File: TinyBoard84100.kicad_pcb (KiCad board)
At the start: 2 copper layers, 14 parts, among them P1 CONN_01X02, P2 CONN_01X07, P3 CONN_01X07, P4 CONN_02X03, SW1 SW_PUSH, U1 78L05, U2 ATTINY841

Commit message: First layout
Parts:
- C1, R1, R2, R3, U1: moved to B.Cu
- moved SW1 37.6 mm to (172.7, 80.0), turned to 270 degrees
- moved C2 35.2 mm to (158.8, 80.0), turned to 90 degrees
- moved R1 33.5 mm to (171.4, 80.0)
- moved C1 33.2 mm to (158.8, 80.0), turned to 90 degrees
- moved U1 29.6 mm to (165.1, 80.0), turned to 180 degrees
- moved U2 29.0 mm to (165.1, 80.0), turned to 90 degrees
- moved D1 28.1 mm to (179.1, 73.7), turned to 180 degrees
- moved P4 25.6 mm to (177.8, 77.5)
- moved R2 24.2 mm to (178.8, 74.4), turned to 180 degrees
- moved P1 24.1 mm to (154.9, 81.3), turned to 180 degrees
- moved R3 24.0 mm to (176.8, 86.4)
- moved P3 20.7 mm to (157.5, 73.7), turned to 90 degrees
- moved D2 18.6 mm to (179.1, 86.4)
- moved P2 6.22 mm to (157.5, 86.4), turned to 90 degrees
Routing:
- net /PA4: track 0.00 -> 22.6 mm, vias 0 -> 1
- net /PB3: track 0.00 -> 22.5 mm, vias 0 -> 2
- net /PA6: track 0.00 -> 16.9 mm, vias 0 -> 1
- net GND: track 0.00 -> 13.4 mm, vias 0 -> 4
- net /PA5: track 0.00 -> 12.0 mm
- net Net-(C1-Pad1): track 0.00 -> 9.79 mm, vias 0 -> 1
- net +5V: track 0.00 -> 8.70 mm, vias 0 -> 1
- net /PA7: track 0.00 -> 4.70 mm
- net /PB0: track 0.00 -> 4.70 mm
- net /PA0: track 0.00 -> 4.70 mm
- net Net-(D1-Pad1): track 0.00 -> 4.64 mm, vias 0 -> 1
- net /PA1: track 0.00 -> 4.18 mm
- net /PB1: track 0.00 -> 4.18 mm
- net /PA3: track 0.00 -> 4.18 mm
- net /PB2: track 0.00 -> 4.18 mm
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- added copper zone on F.Cu, net +5V
- added copper zone on B.Cu, net GND
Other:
- board outline added: 27.9 x 15.2 mm

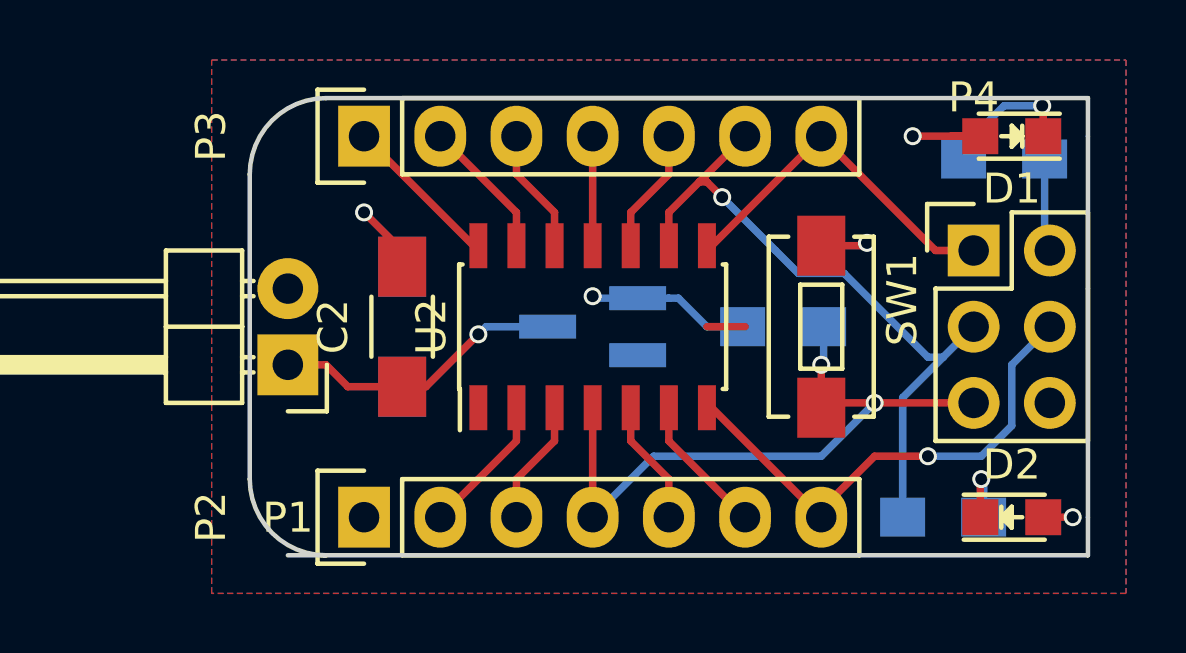
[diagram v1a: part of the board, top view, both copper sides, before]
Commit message: fixed zone connections
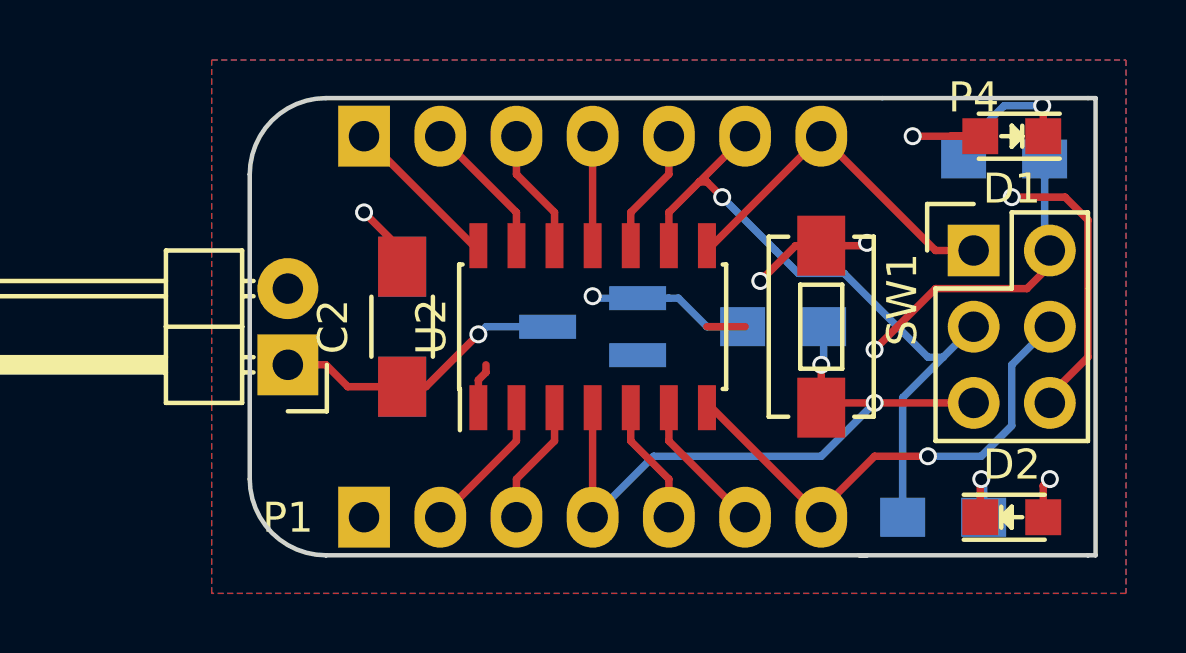
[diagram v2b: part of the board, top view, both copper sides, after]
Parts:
- P2, P3: moved to B.Cu
- turned P2 to 270 degrees
- turned P3 to 270 degrees
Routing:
- net GND: track 13.4 -> 25.8 mm, vias 4 -> 6
- net +5V: track 8.70 -> 17.7 mm, vias 1 -> 2
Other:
- board size 27.9 x 15.2 mm -> 28.2 x 15.2 mm

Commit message: gerbers
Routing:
- net (no net): track 1.27 -> 0.00 mm
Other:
- board text added: "+ -"
- board text added: "5V"
- board text added: "GND"
- board text added: "PA0"
- board text added: "PA1"
- board text added: "PA2"
- board text added: "PA3"
- board text added: "PA4"
- board text added: "PA5"
- board text added: "PA6"
- board text added: "PA7"
- board text added: "PB0"
- board text added: "PB1"
- board text added: "PB2"
- board text added: "PB3"
- board text added: "TinyBoard84100"

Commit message: silkscreen edits
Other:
- board text added: "+"
- board text added: "-"
- board text added: "TinyBoard84100 Unregulated Powersupply Rev2"
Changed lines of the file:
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@@
     (links 38)
     (no_connects 1)
-    (area 143.810667 68.875 185.453143 91.393333)
+    (area 153.594999 72.314999 181.939001 87.705001)
     (thickness 1.6)
-    (drawings 26)
+    (drawings 29)
     (tracks 119)
     (zones 0)
@@
   (page A4)
   (layers
-    (0 F.Cu signal hide)
-    (31 B.Cu signal hide)
+    (0 F.Cu signal)
+    (31 B.Cu signal)
     (32 B.Adhes user hide)
     (33 F.Adhes user hide)
@@
     (tags "LED 0805 SMD")
     (attr smd)
-    (fp_text reference D1 (at 2.54 0.254 180) (layer F.SilkS)
+    (fp_text reference D1 (at 0 2.032 180) (layer F.SilkS)
       (effects (font (size 1 1) (thickness 0.15)))
     )
@@
     (tags "LED 0805 SMD")
     (attr smd)
-    (fp_text reference D2 (at 0 -1.524) (layer F.SilkS)
+    (fp_text reference D2 (at -2.54 2.54) (layer F.SilkS)
       (effects (font (size 1 1) (thickness 0.15)))
     )
@@
     )
   )
+  (gr_text - (at 180.594 84.328) (layer F.SilkS)
+    (effects (font (size 0.762 0.762) (thickness 0.1905)))
+  )
+  (gr_text + (at 180.34 75.692) (layer F.SilkS)
+    (effects (font (size 0.762 0.762) (thickness 0.1905)))
+  )
+  (gr_text "TinyBoard84100\nUnregulated\nPowersupply\nRev2" (at 167.894 80.264) (layer B.SilkS)
+    (effects (font (thickness 0.3048)) (justify mirror))
+  )
   (gr_text "+  -" (at 156.972 80.01 90) (layer F.SilkS)

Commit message: minimizing
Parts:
- removed P1: CONN_01X02, Pin_Headers:Pin_Header_Angled_1x02
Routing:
- net Net-(C1-Pad1): track 9.79 -> 5.68 mm
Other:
- board size 28.2 x 15.2 mm -> 25.7 x 15.2 mm
- board text removed: "+ -"
- board text removed: "TinyBoard84100 Unregulated Powersupply Rev2"
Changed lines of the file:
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@@
 (kicad_pcb (version 4) (host pcbnew 4.0.5+dfsg1-4)
   (general
-    (links 38)
+    (links 36)
     (no_connects 1)
-    (area 153.594999 72.314999 181.939001 87.705001)
+    (area 156.134999 72.314999 181.939001 87.705001)
     (thickness 1.6)
-    (drawings 29)
-    (tracks 119)
+    (drawings 26)
+    (tracks 116)
     (zones 0)
-    (modules 14)
+    (modules 13)
     (nets 18)
   )
   (page A4)
   (layers
-    (0 F.Cu signal)
-    (31 B.Cu signal)
+    (0 F.Cu signal hide)
+    (31 B.Cu signal hide)
     (32 B.Adhes user hide)
     (33 F.Adhes user hide)
@@
     (35 F.Paste user hide)
     (36 B.SilkS user)
-    (37 F.SilkS user)
+    (37 F.SilkS user hide)
     (38 B.Mask user hide)
     (39 F.Mask user hide)
@@
     (pad_to_mask_clearance 0.2)
     (aux_axis_origin 0 0)
-    (grid_origin 153.924 72.644)
+    (grid_origin 156.21 72.39)
     (visible_elements FFFFFF7F)
     (pcbplotparams
@@
       (scale (xyz 1 1 1))
       (rotate (xyz 0 0 0))
-    )
-  )
-  (module Pin_Headers:Pin_Header_Angled_1x02 (layer F.Cu)
-    (at 154.94 81.28 180)
-    (descr "Through hole pin header")
-    (tags "pin header")
-    (fp_text reference P1 (at -0.508 -7.112 180) (layer F.SilkS)
-      (effects (font (size 1 1) (thickness 0.15)))
-    )
-    (fp_text value CONN_01X02 (at 6.096 -6.096 180) (layer F.Fab)
-      (effects (font (size 1 1) (thickness 0.15)))
-    )
-    (fp_line (start -1.5 -1.75) (end -1.5 4.3) (layer F.CrtYd) (width 0.05))
-    (fp_line (start 10.65 -1.75) (end 10.65 4.3) (layer F.CrtYd) (width 0.05))
-    (fp_line (start -1.5 -1.75) (end 10.65 -1.75) (layer F.CrtYd) (width 0.05))
-    (fp_line (start -1.5 4.3) (end 10.65 4.3) (layer F.CrtYd) (width 0.05))
-    (fp_line (start -1.3 -1.55) (end -1.3 0) (layer F.SilkS) (width 0.15))
-    (fp_line (start 0 -1.55) (end -1.3 -1.55) (layer F.SilkS) (width 0.15))
-    (fp_line (start 4.191 -0.127) (end 10.033 -0.127) (layer F.SilkS) (width 0.15))
-    (fp_line (start 10.033 -0.127) (end 10.033 0.127) (layer F.SilkS) (width 0.15))
-    (fp_line (start 10.033 0.127) (end 4.191 0.127) (layer F.SilkS) (width 0.15))
-    (fp_line (start 4.191 0.127) (end 4.191 0) (layer F.SilkS) (width 0.15))
-    (fp_line (start 4.191 0) (end 10.033 0) (layer F.SilkS) (width 0.15))
-    (fp_line (start 1.524 -0.254) (end 1.143 -0.254) (layer F.SilkS) (width 0.15))
-    (fp_line (start 1.524 0.254) (end 1.143 0.254) (layer F.SilkS) (width 0.15))
-    (fp_line (start 1.524 2.286) (end 1.143 2.286) (layer F.SilkS) (width 0.15))
-    (fp_line (start 1.524 2.794) (end 1.143 2.794) (layer F.SilkS) (width 0.15))
-    (fp_line (start 1.524 -1.27) (end 4.064 -1.27) (layer F.SilkS) (width 0.15))
-    (fp_line (start 1.524 1.27) (end 4.064 1.27) (layer F.SilkS) (width 0.15))
-    (fp_line (start 1.524 1.27) (end 1.524 3.81) (layer F.SilkS) (width 0.15))
-    (fp_line (start 1.524 3.81) (end 4.064 3.81) (layer F.SilkS) (width 0.15))
-    (fp_line (start 4.064 2.286) (end 10.16 2.286) (layer F.SilkS) (width 0.15))
-    (fp_line (start 10.16 2.286) (end 10.16 2.794) (layer F.SilkS) (width 0.15))
-    (fp_line (start 10.16 2.794) (end 4.064 2.794) (layer F.SilkS) (width 0.15))
-    (fp_line (start 4.064 3.81) (end 4.064 1.27) (layer F.SilkS) (width 0.15))
-    (fp_line (start 4.064 1.27) (end 4.064 -1.27) (layer F.SilkS) (width 0.15))
-    (fp_line (start 10.16 0.254) (end 4.064 0.254) (layer F.SilkS) (width 0.15))
-    (fp_line (start 10.16 -0.254) (end 10.16 0.254) (layer F.SilkS) (width 0.15))
-    (fp_line (start 4.064 -0.254) (end 10.16 -0.254) (layer F.SilkS) (width 0.15))
-    (fp_line (start 1.524 1.27) (end 4.064 1.27) (layer F.SilkS) (width 0.15))
-    (fp_line (start 1.524 -1.27) (end 1.524 1.27) (layer F.SilkS) (width 0.15))
-    (pad 1 thru_hole rect (at 0 0 180) (size 2.032 2.032) (drill 1.016) (layers *.Cu *.Mask)
-      (net 1 "Net-(C1-Pad1)"))
-    (pad 2 thru_hole oval (at 0 2.54 180) (size 2.032 2.032) (drill 1.016) (layers *.Cu *.Mask)
-      (net 2 GND))
-    (model Pin_Headers.3dshapes/Pin_Header_Angled_1x02.wrl
-      (at (xyz 0 -0.05 0))
-      (scale (xyz 1 1 1))
-      (rotate (xyz 0 0 90))
     )
   )
@@
     )
   )
+  (gr_line (start 156.21 72.39) (end 156.21 87.63) (angle 90) (layer Edge.Cuts) (width 0.15))
   (gr_text - (at 180.594 84.328) (layer F.SilkS)
     (effects (font (size 0.762 0.762) (thickness 0.1905)))
@@
     (effects (font (size 0.762 0.762) (thickness 0.1905)))
   )
-  (gr_text "TinyBoard84100\nUnregulated\nPowersupply\nRev2" (at 167.894 80.264) (layer B.SilkS)
+  (gr_text TinyBoard84100 (at 167.894 76.454) (layer B.SilkS)
     (effects (font (thickness 0.3048)) (justify mirror))
-  )
-  (gr_text "+  -" (at 156.972 80.01 90) (layer F.SilkS)
-    (effects (font (size 1.016 1.016) (thickness 0.1905)))
   )
   (gr_text PA6 (at 172.72 84.328 180) (layer F.SilkS)
@@
   (gr_line (start 156.21 72.39) (end 174.752 72.39) (angle 90) (layer Edge.Cuts) (width 0.15))
   (gr_line (start 156.21 87.63) (end 174.244 87.63) (angle 90) (layer Edge.Cuts) (width 0.15))
-  (gr_arc (start 156.21 85.09) (end 156.21 87.63) (angle 90) (layer Edge.Cuts) (width 0.15))
-  (gr_arc (start 156.21 74.93) (end 153.67 74.93) (angle 90) (layer Edge.Cuts) (width 0.15))
-  (gr_line (start 153.67 74.93) (end 153.67 85.09) (angle 90) (layer Edge.Cuts) (width 0.15))
   (segment (start 158.75 82.01) (end 159.544 82.01) (width 0.25) (layer F.Cu) (net 1))
   (segment (start 159.544 82.01) (end 161.29 80.264) (width 0.25) (layer F.Cu) (net 1))
@@
   (segment (start 161.29 80.264) (end 161.544 80.01) (width 0.25) (layer B.Cu) (net 1))
   (via (at 161.29 80.264) (size 0.6) (drill 0.4) (layers F.Cu B.Cu) (net 1))
-  (segment (start 154.94 81.28) (end 156.21 81.28) (width 0.25) (layer F.Cu) (net 1))
-  (segment (start 156.94 82.01) (end 158.75 82.01) (width 0.25) (layer F.Cu) (net 1))
-  (segment (start 156.21 81.28) (end 156.94 82.01) (width 0.25) (layer F.Cu) (net 1))
   (segment (start 180.34 82.55) (end 180.34 82.296) (width 0.25) (layer F.Cu) (net 2))
   (segment (start 180.34 82.296) (end 181.61 81.026) (width 0.25) (layer F.Cu) (net 2))

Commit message: various exports
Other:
- board text added: "04/18"
- board text added: "Rev2"
- board text added: "Unregulated Powersupply"
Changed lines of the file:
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@@
     (area 156.134999 72.314999 181.939001 87.705001)
     (thickness 1.6)
-    (drawings 26)
+    (drawings 29)
     (tracks 116)
     (zones 0)
@@
   (page A4)
   (layers
-    (0 F.Cu signal hide)
-    (31 B.Cu signal hide)
+    (0 F.Cu signal)
+    (31 B.Cu signal)
     (32 B.Adhes user hide)
     (33 F.Adhes user hide)
@@
     (35 F.Paste user hide)
     (36 B.SilkS user)
-    (37 F.SilkS user hide)
+    (37 F.SilkS user)
     (38 B.Mask user hide)
     (39 F.Mask user hide)
@@
     (tags "LED 0805 SMD")
     (attr smd)
-    (fp_text reference D1 (at 0 2.032 180) (layer F.SilkS)
-      (effects (font (size 1 1) (thickness 0.15)))
-    )
-    (fp_text value LED (at -4.826 3.302 180) (layer F.Fab)
+    (fp_text reference D1 (at 0 2.032 180) (layer F.SilkS) hide
+      (effects (font (size 1 1) (thickness 0.15)))
+    )
+    (fp_text value LED (at -4.826 3.302 180) (layer F.Fab) hide
       (effects (font (size 1 1) (thickness 0.15)))
     )
@@
     (tags "LED 0805 SMD")
     (attr smd)
-    (fp_text reference D2 (at -2.54 2.54) (layer F.SilkS)
-      (effects (font (size 1 1) (thickness 0.15)))
-    )
-    (fp_text value LED (at 0.508 2.54) (layer F.Fab)
+    (fp_text reference D2 (at -2.54 2.54) (layer F.SilkS) hide
+      (effects (font (size 1 1) (thickness 0.15)))
+    )
+    (fp_text value LED (at 0.508 2.54) (layer F.Fab) hide
       (effects (font (size 1 1) (thickness 0.15)))
     )
@@
     (descr "Through hole pin header")
     (tags "pin header")
-    (fp_text reference P2 (at 0 5.1 270) (layer B.SilkS)
-      (effects (font (size 1 1) (thickness 0.15)) (justify mirror))
-    )
-    (fp_text value CONN_01X07 (at 0 5.334 270) (layer B.Fab)
+    (fp_text reference P2 (at 0 5.1 270) (layer B.SilkS) hide
+      (effects (font (size 1 1) (thickness 0.15)) (justify mirror))
+    )
+    (fp_text value CONN_01X07 (at 0 5.334 270) (layer B.Fab) hide
       (effects (font (size 1 1) (thickness 0.15)) (justify mirror))
     )
@@
     (descr "Through hole pin header")
     (tags "pin header")
-    (fp_text reference P3 (at 0 5.1 270) (layer B.SilkS)
-      (effects (font (size 1 1) (thickness 0.15)) (justify mirror))
-    )
-    (fp_text value CONN_01X07 (at 0.254 5.334 270) (layer B.Fab)
+    (fp_text reference P3 (at 0 5.1 270) (layer B.SilkS) hide
+      (effects (font (size 1 1) (thickness 0.15)) (justify mirror))
+    )
+    (fp_text value CONN_01X07 (at 0.254 5.334 270) (layer B.Fab) hide
       (effects (font (size 1 1) (thickness 0.15)) (justify mirror))
     )
@@
     (descr "Through hole pin header")
     (tags "pin header")
-    (fp_text reference P4 (at 6.35 -4.064) (layer F.SilkS)
-      (effects (font (size 1 1) (thickness 0.15)))
-    )
-    (fp_text value CONN_02X03 (at -0.254 -7.62) (layer F.Fab)
+    (fp_text reference P4 (at 6.35 -4.064) (layer F.SilkS) hide
+      (effects (font (size 1 1) (thickness 0.15)))
+    )
+    (fp_text value CONN_02X03 (at -0.254 -7.62) (layer F.Fab) hide
       (effects (font (size 1 1) (thickness 0.15)))
     )
@@
       (effects (font (size 1 1) (thickness 0.15)) (justify mirror))
     )
-    (fp_text value 1k (at -5.334 -1.016 180) (layer B.Fab)
+    (fp_text value 1k (at -5.334 -1.016 180) (layer B.Fab) hide
       (effects (font (size 1 1) (thickness 0.15)) (justify mirror))
     )
@@
       (effects (font (size 1 1) (thickness 0.15)) (justify mirror))
     )
-    (fp_text value 1k (at -2.794 3.048) (layer B.Fab)
+    (fp_text value 1k (at -2.794 3.048) (layer B.Fab) hide
       (effects (font (size 1 1) (thickness 0.15)) (justify mirror))
     )
@@
       (rotate (xyz 0 0 0))
     )
+  )
+  (gr_text 04/18 (at 156.845 80.01 90) (layer B.SilkS)
+    (effects (font (size 0.508 0.508) (thickness 0.127)) (justify mirror))
+  )
+  (gr_text Rev2 (at 175.768 80.264 90) (layer B.SilkS)
+    (effects (font (size 0.762 0.762) (thickness 0.1905)) (justify mirror))
+  )
+  (gr_text "Unregulated Powersupply" (at 167.386 84.074) (layer B.SilkS)
+    (effects (font (size 1.016 1.016) (thickness 0.254)) (justify mirror))
   )
   (gr_line (start 156.21 72.39) (end 156.21 87.63) (angle 90) (layer Edge.Cuts) (width 0.15))
@@
     (polygon
       (pts
-        (xy 182.88 88.9) (xy 152.4 88.9) (xy 152.4 71.12) (xy 182.88 71.12)
+        (xy 182.88 88.9) (xy 154.94 88.9) (xy 154.94 71.12) (xy 182.88 71.12)
       )
     )
@@
     (polygon
       (pts
-        (xy 182.88 88.9) (xy 152.4 88.9) (xy 152.4 71.12) (xy 182.88 71.12)
+        (xy 182.88 88.9) (xy 154.94 88.9) (xy 154.94 71.12) (xy 182.88 71.12)
       )
     )
